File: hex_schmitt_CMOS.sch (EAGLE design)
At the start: 8 parts, among them IC1 40106N, J1 AUDIO_JACK_3.5MM_PTH

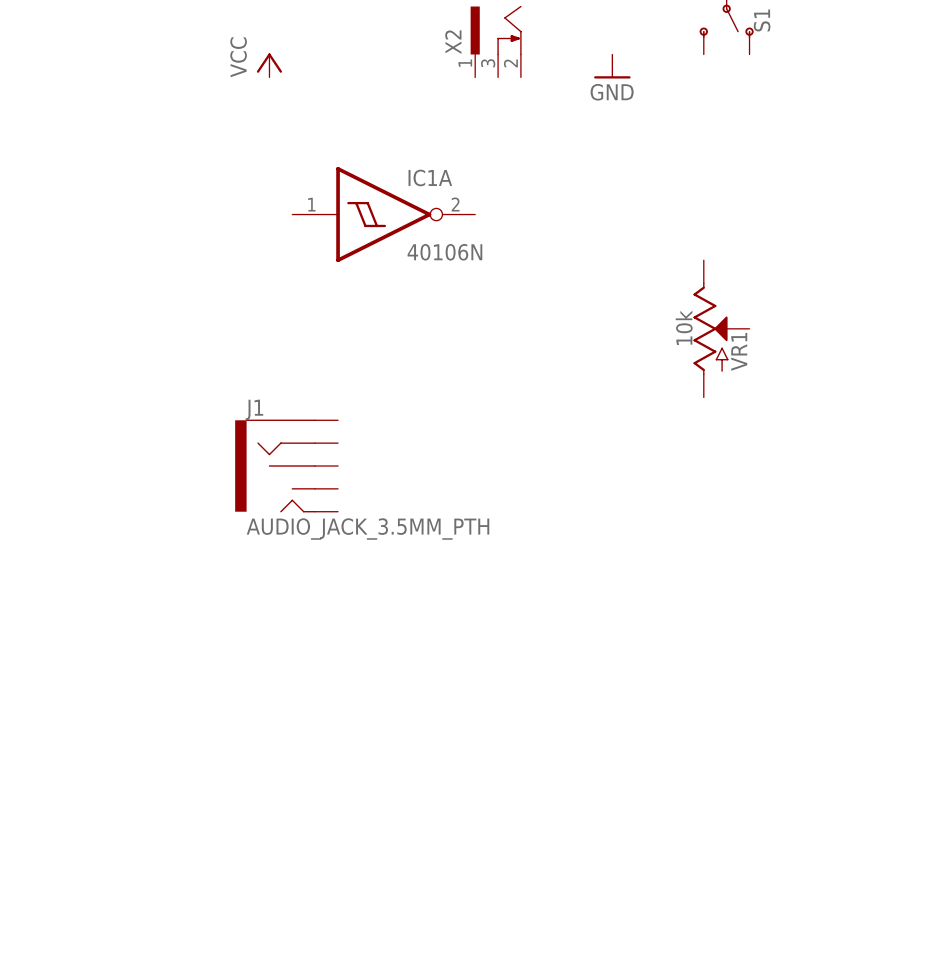
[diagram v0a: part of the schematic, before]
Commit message: adds all 40106 pins to .sch
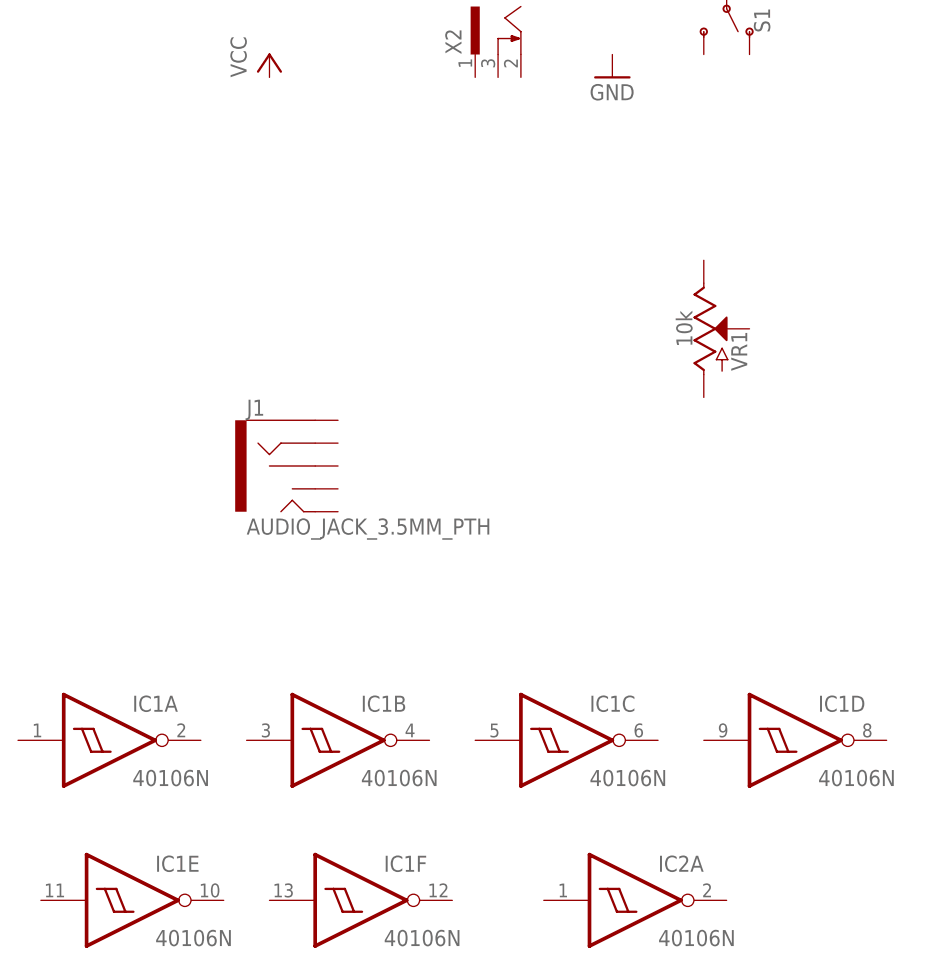
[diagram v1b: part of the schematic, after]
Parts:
- added IC2: 40106N, 40xx:40106N
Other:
- moved on the sheet: IC1A
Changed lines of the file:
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@@
 </classes>
 <parts>
-<part name="IC1" library="40xx" library_urn="urn:adsk.eagle:library:80" deviceset="40106" device="N" package3d_urn="urn:adsk.eagle:package:16407/2"/>
 <part name="P+1" library="supply1" library_urn="urn:adsk.eagle:library:371" deviceset="VCC" device=""/>
 <part name="GND1" library="supply1" library_urn="urn:adsk.eagle:library:371" deviceset="GND" device=""/>
@@
 <part name="R1" library="resistor" library_urn="urn:adsk.eagle:library:348" deviceset="R-US_" device="0204/5" package3d_urn="urn:adsk.eagle:package:25955/1"/>
 <part name="LED1" library="led" library_urn="urn:adsk.eagle:library:259" deviceset="LED" device="5MM" package3d_urn="urn:adsk.eagle:package:15799/2"/>
+<part name="IC1" library="40xx" library_urn="urn:adsk.eagle:library:80" deviceset="40106" device="N" package3d_urn="urn:adsk.eagle:package:16407/2"/>
+<part name="IC2" library="40xx" library_urn="urn:adsk.eagle:library:80" deviceset="40106" device="N" package3d_urn="urn:adsk.eagle:package:16407/2"/>
 </parts>
 <sheets>
@@
 </plain>
 <instances>
-<instance part="IC1" gate="A" x="71.12" y="40.64" smashed="yes">
-<attribute name="NAME" x="73.66" y="43.815" size="1.778" layer="95"/>
-<attribute name="VALUE" x="73.66" y="35.56" size="1.778" layer="96"/>
-</instance>
 <instance part="P+1" gate="VCC" x="58.42" y="58.42" smashed="yes">
 <attribute name="VALUE" x="55.88" y="55.88" size="1.778" layer="96" rot="R90"/>
@@
 <attribute name="VALUE" x="99.695" y="66.548" size="1.778" layer="96" rot="R90"/>
 </instance>
+<instance part="IC1" gate="A" x="40.64" y="-17.78" smashed="yes">
+<attribute name="NAME" x="43.18" y="-14.605" size="1.778" layer="95"/>
+<attribute name="VALUE" x="43.18" y="-22.86" size="1.778" layer="96"/>
+</instance>
+<instance part="IC1" gate="B" x="66.04" y="-17.78" smashed="yes">
+<attribute name="NAME" x="68.58" y="-14.605" size="1.778" layer="95"/>
+<attribute name="VALUE" x="68.58" y="-22.86" size="1.778" layer="96"/>
+</instance>
+<instance part="IC1" gate="C" x="91.44" y="-17.78" smashed="yes">
+<attribute name="NAME" x="93.98" y="-14.605" size="1.778" layer="95"/>
+<attribute name="VALUE" x="93.98" y="-22.86" size="1.778" layer="96"/>
+</instance>
+<instance part="IC1" gate="D" x="116.84" y="-17.78" smashed="yes">
+<attribute name="NAME" x="119.38" y="-14.605" size="1.778" layer="95"/>
+<attribute name="VALUE" x="119.38" y="-22.86" size="1.778" layer="96"/>
+</instance>
+<instance part="IC1" gate="E" x="43.18" y="-35.56" smashed="yes">
+<attribute name="NAME" x="45.72" y="-32.385" size="1.778" layer="95"/>
+<attribute name="VALUE" x="45.72" y="-40.64" size="1.778" layer="96"/>
+</instance>
+<instance part="IC1" gate="F" x="68.58" y="-35.56" smashed="yes">
+<attribute name="NAME" x="71.12" y="-32.385" size="1.778" layer="95"/>
+<attribute name="VALUE" x="71.12" y="-40.64" size="1.778" layer="96"/>
+</instance>
+<instance part="IC2" gate="A" x="99.06" y="-35.56" smashed="yes">
+<attribute name="NAME" x="101.6" y="-32.385" size="1.778" layer="95"/>
+<attribute name="VALUE" x="101.6" y="-40.64" size="1.778" layer="96"/>
+</instance>
 </instances>

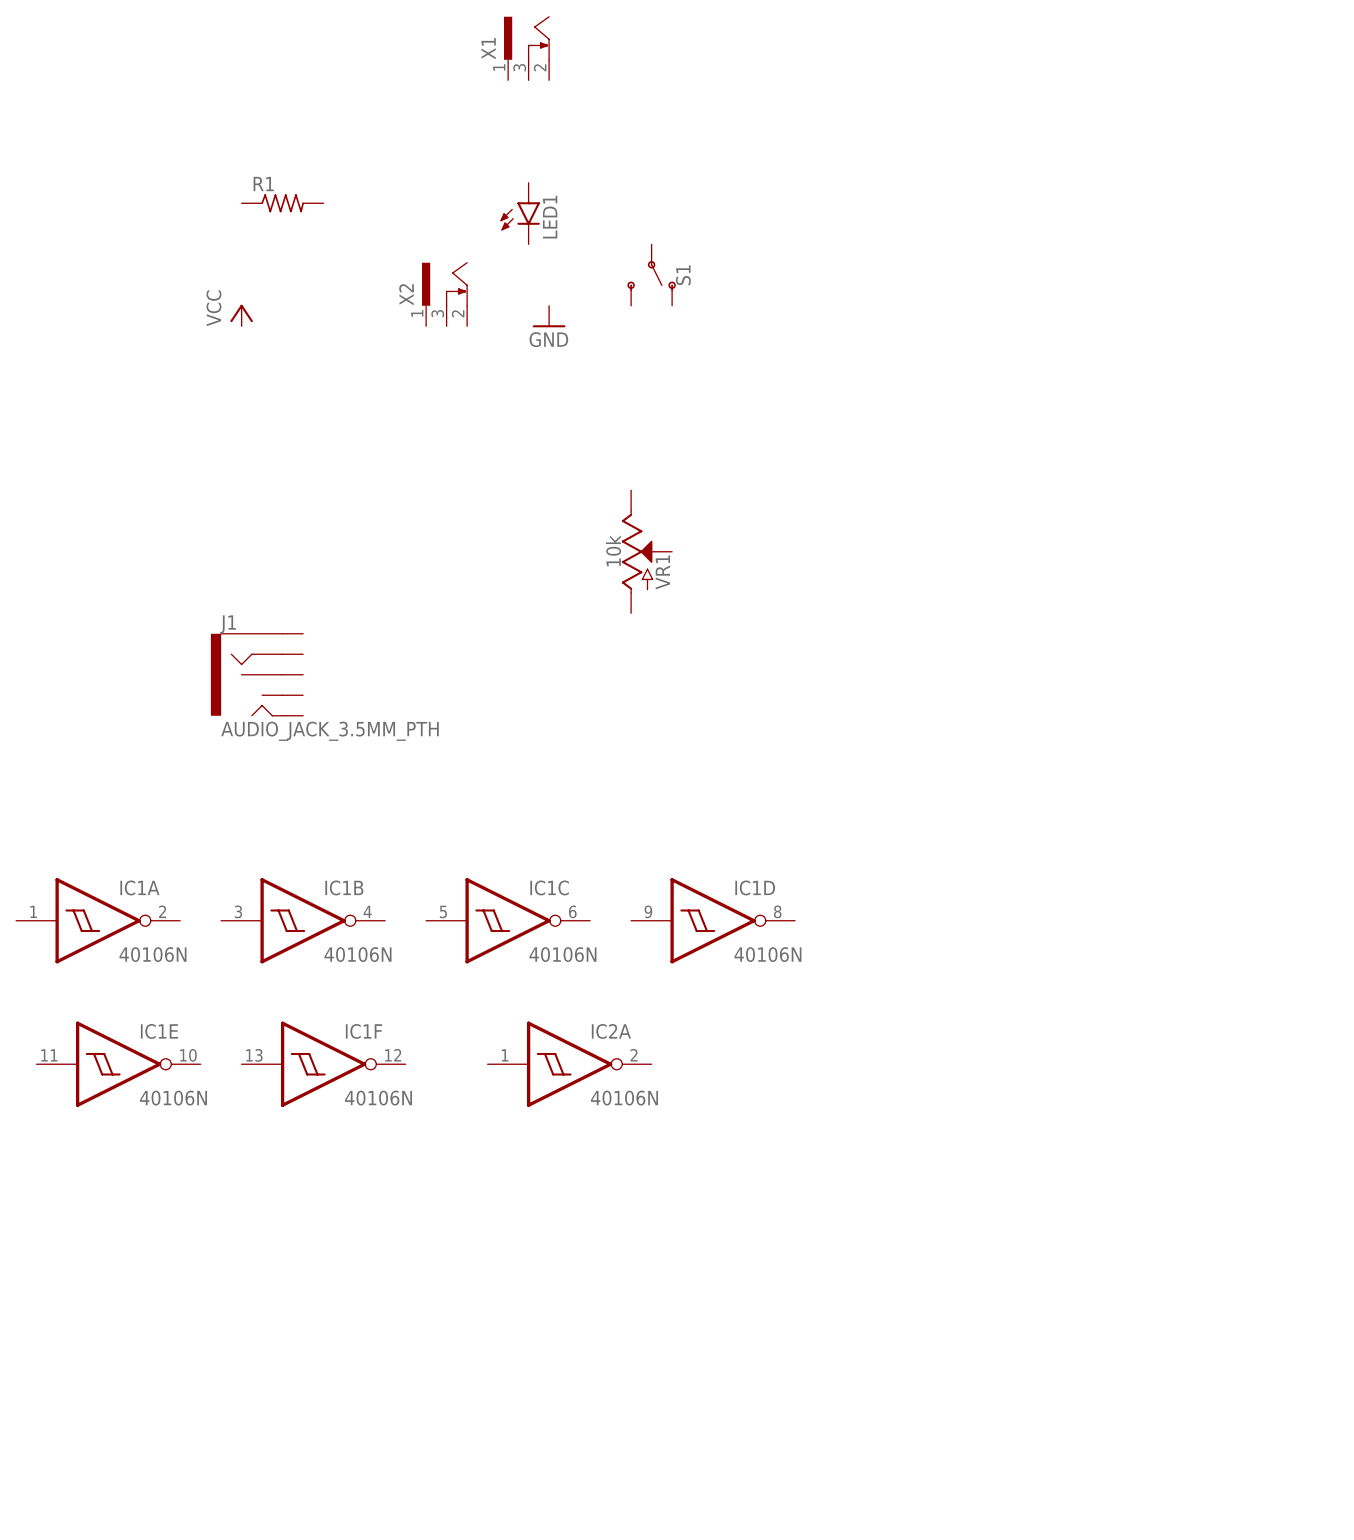
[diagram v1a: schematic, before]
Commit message: adds completed 1st draft of schematic, adds .brd file
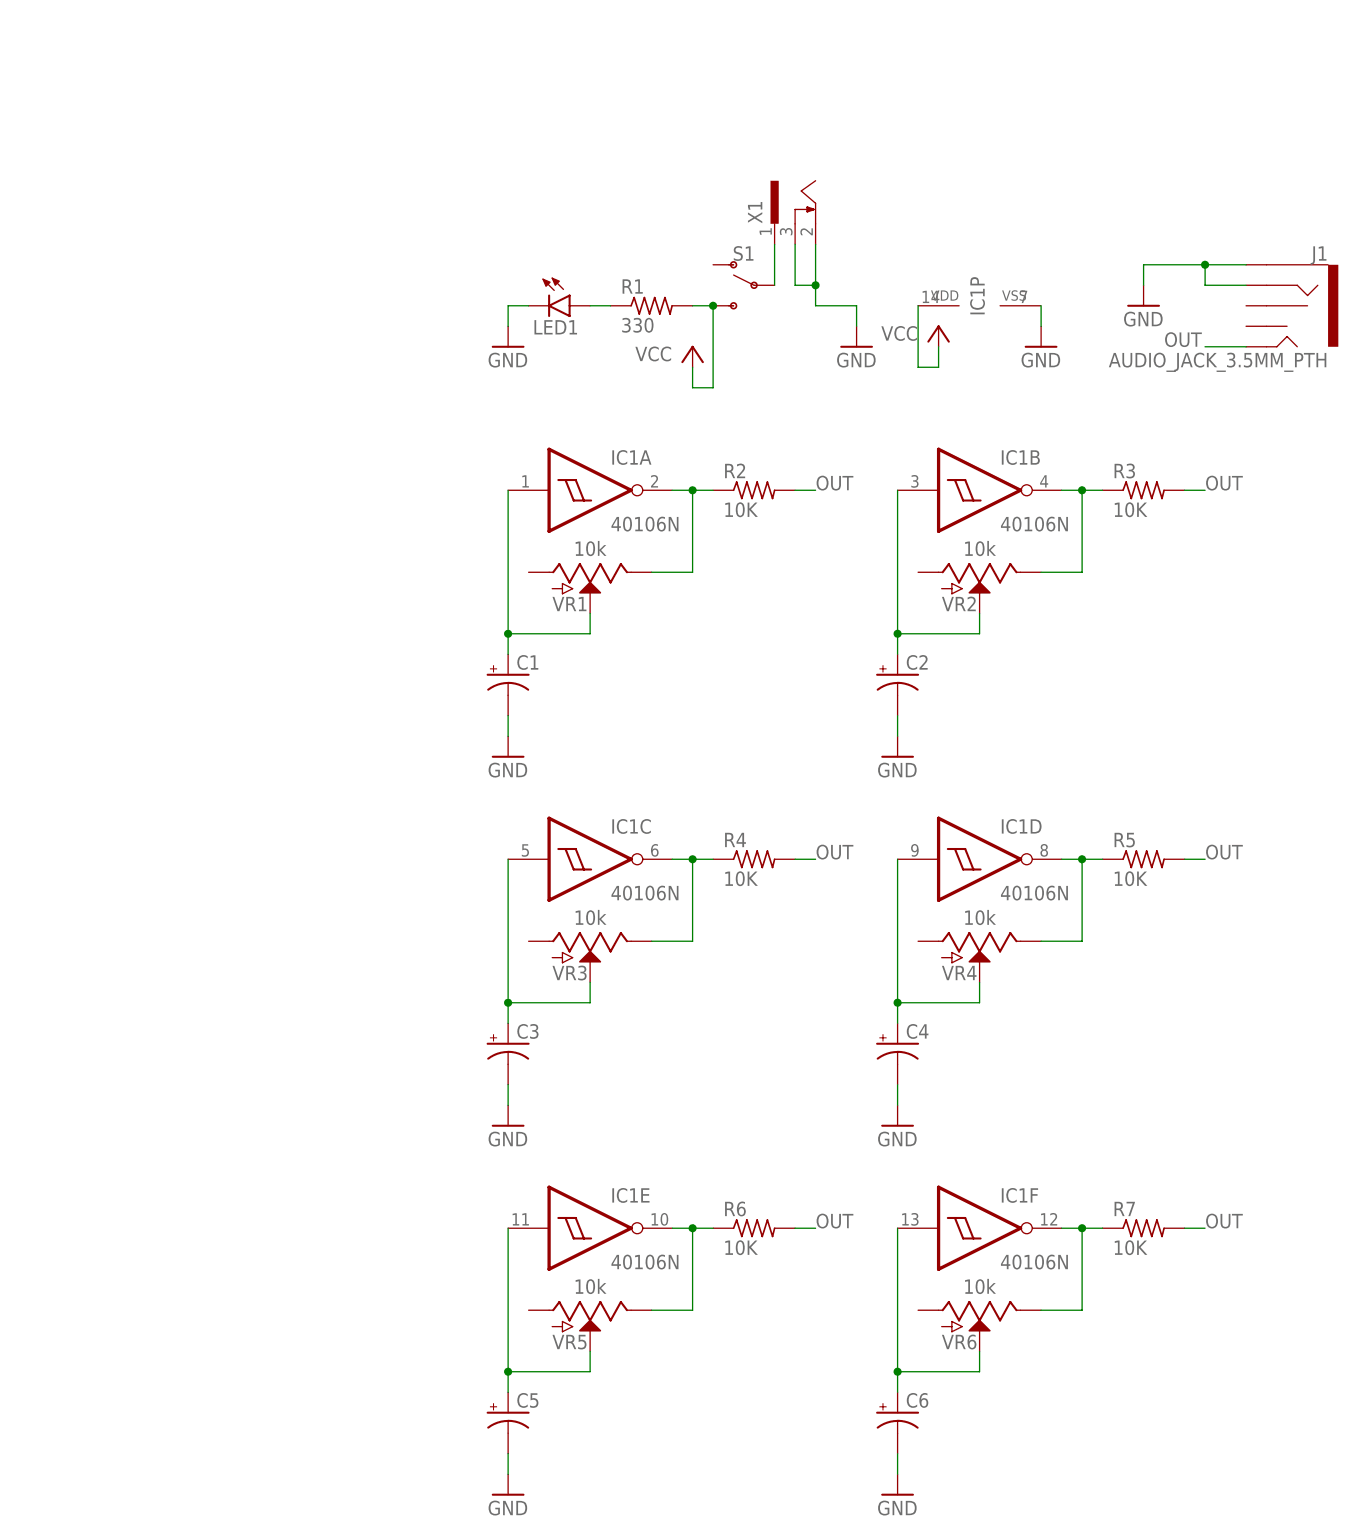
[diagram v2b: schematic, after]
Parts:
- removed IC2: 40106N, 40xx:40106N
- removed X2: (no value), con-shiua-chyuan:SCD-014A
- added C1, C2, C3, C4, C5, C6: (no value), resistor:CPOL-USE1.8-4
- added R2, R3, R4, R5, R6, R7: 10K, resistor:R-US_0204/5
- added VR2, VR3, VR4, VR5, VR6: 10k, SparkFun-Resistors:POTENTIOMETER-PTH-9MM-1/20W-20%
- R1: value (none) -> 330
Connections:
- new net GND: C1.-, C2.-, C3.-, C4.-, C5.-, C6.-, IC1P.VSS, J1.RING, J1.SLEEVE, LED1.C, X1.2, X1.3
- new net N$1: S1.P, X1.1
- new net N$10: IC1D.O, R5.1, VR4.E
- new net N$11: C5.+, IC1E.I, VR5.S
- new net N$12: IC1E.O, R6.1, VR5.E
- new net N$13: C6.+, IC1F.I, VR6.S
- new net N$14: IC1F.O, R7.1, VR6.E
- new net N$2: C1.+, IC1A.I, VR1.S
- new net N$3: LED1.A, R1.1
- new net N$4: IC1A.O, R2.1, VR1.E
- new net N$5: C2.+, IC1B.I, VR2.S
- new net N$6: IC1B.O, R3.1, VR2.E
- new net N$7: C3.+, IC1C.I, VR3.S
- new net N$8: IC1C.O, R4.1, VR3.E
- new net N$9: C4.+, IC1D.I, VR4.S
- new net OUT: J1.TIP, R2.2, R3.2, R4.2, R5.2, R6.2, R7.2
- new net VCC: IC1P.VDD, R1.2, S1.S
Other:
- moved on the sheet: IC1A, IC1B, IC1C, IC1D, IC1E, IC1F, J1, LED1, R1, S1, VR1, X1

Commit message: v1, single oscillator pcb works
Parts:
- removed C2, C3, C4, C5, C6: (no value), resistor:CPOL-USE1.8-4
- removed R3, R4, R5, R6, R7: 10K, resistor:R-US_0204/5
- removed VR2, VR3, VR4, VR5, VR6: 10k, SparkFun-Resistors:POTENTIOMETER-PTH-9MM-1/20W-20%
- added H1, H2, H3, H4: STAND-OFF, SparkFun-Hardware:STAND-OFF
- C1: value (none) -> 10u; device resistor:CPOL-USE1.8-4 -> cta_library_EAGLE:CPOL-USE2.5-5
- LED1: value (none) -> Red
- R1: value 330 -> 10k; device resistor:R-US_0204/5 -> cta_library_EAGLE:R-US_0204/5
- R2: value 10K -> 330; device resistor:R-US_0204/5 -> cta_library_EAGLE:R-US_0204/5
- S1: value (none) -> switch
- X1: value (none) -> DC
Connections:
- removed net N$10: IC1D.O, R5.1, VR4.E
- removed net N$11: C5.+, IC1E.I, VR5.S
- removed net N$12: IC1E.O, R6.1, VR5.E
- removed net N$13: C6.+, IC1F.I, VR6.S
- removed net N$14: IC1F.O, R7.1, VR6.E
- removed net N$3 (its old number): LED1.A, R1.1
- removed net N$4: IC1A.O, R2.1, VR1.E
- removed net N$6: IC1B.O, R3.1, VR2.E
- removed net N$7: C3.+, IC1C.I, VR3.S
- removed net N$8: IC1C.O, R4.1, VR3.E
- removed net N$9: C4.+, IC1D.I, VR4.S
- new net N$2: IC1A.O, R1.1, VR1.E
- net GND: no longer C2.-, C3.-, C4.-, C5.-, C6.-
- net N$5: now also LED1.A, R2.1; no longer C2.+, IC1B.I, VR2.S
- net OUT: now also R1.2; no longer R2.2, R3.2, R4.2, R5.2, R6.2, R7.2
- net VCC: now also R2.2; no longer R1.2
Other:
- moved on the sheet: IC1B, IC1C, IC1D, IC1E, IC1F, IC1P, R1, R2
